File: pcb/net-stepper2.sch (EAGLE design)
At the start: 37 parts, among them IC2 CP2104, J1 MICRO-USB, J2 POWER_JACKPTH_LOCK, J3 ENCODER, J4 ENDSTOP2, J5 ENDSTOP1, J6 STEPER, Q1 600mA/40V, Q2 600mA/40V, U1 L6470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

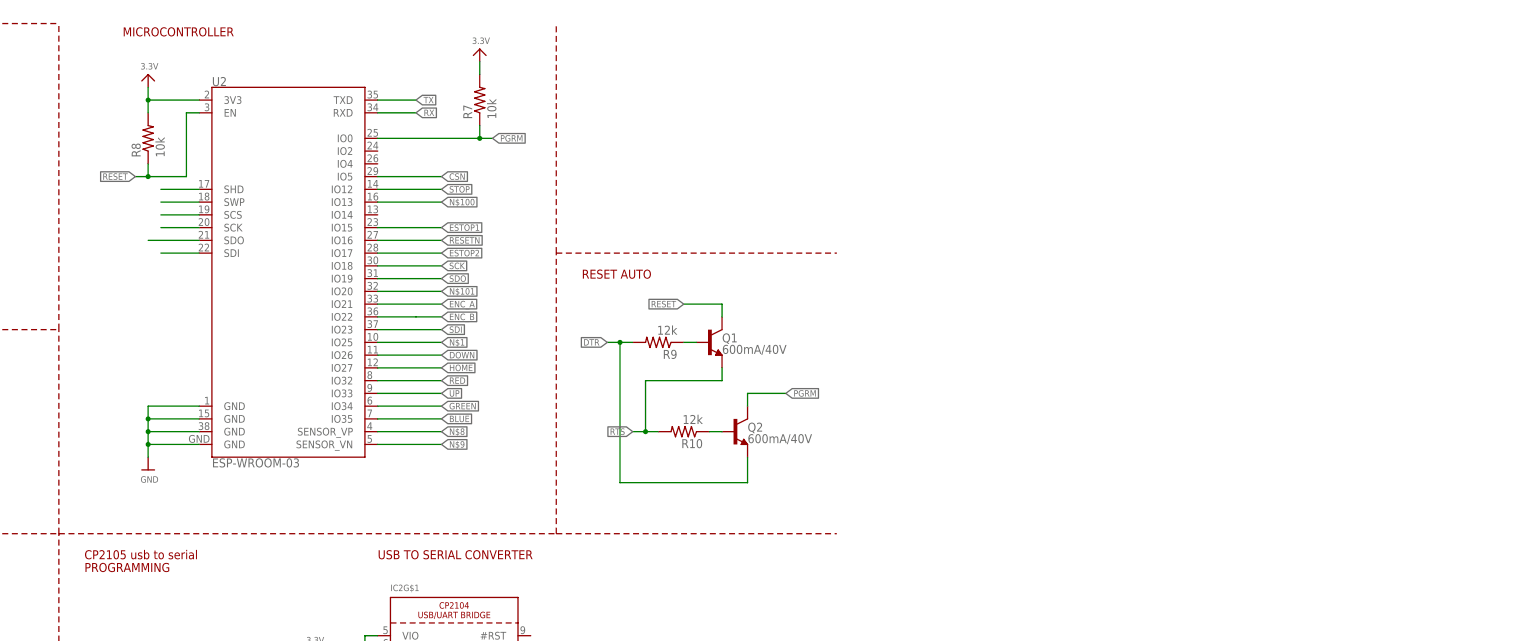
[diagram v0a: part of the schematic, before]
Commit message: replaced esp32 component
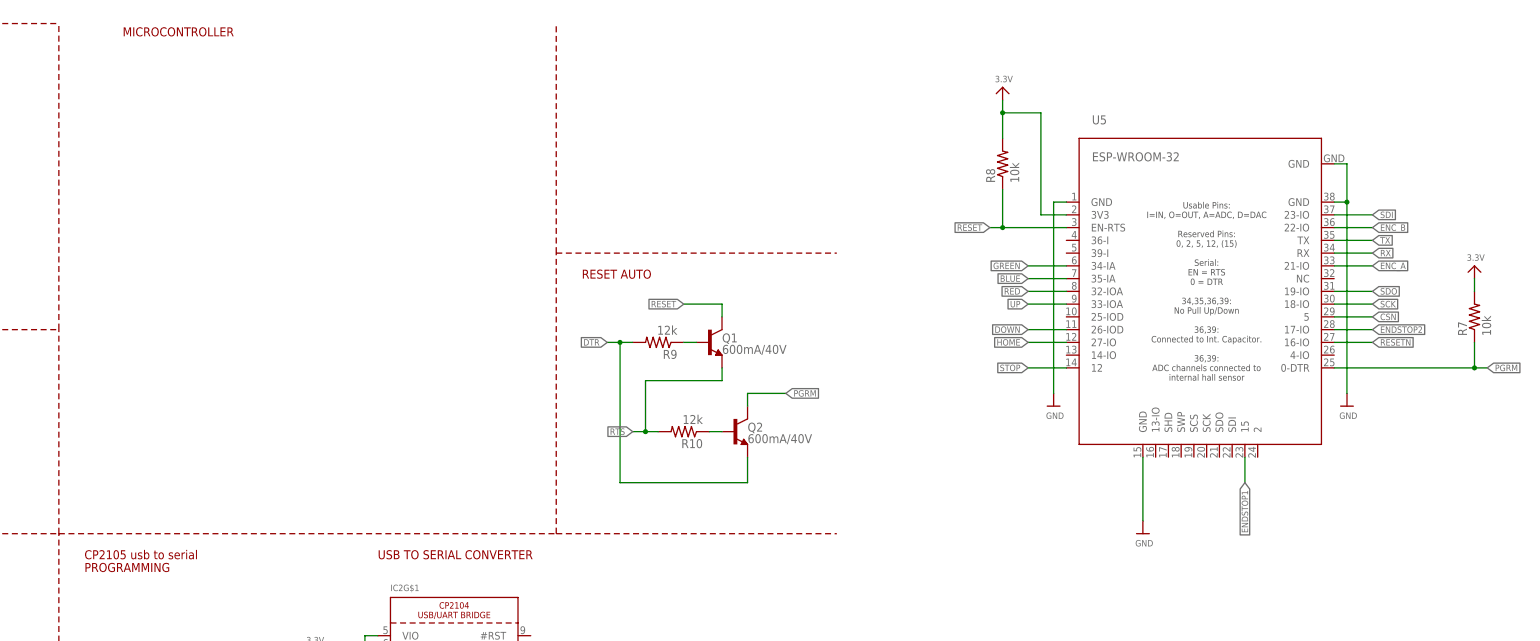
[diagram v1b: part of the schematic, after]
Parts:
- removed U2: ESP-WROOM-03, esp32:ESP-WROOM-03
- added U5: ESP-WROOM-32, esp32:ESP-WROOM-32
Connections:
- removed net ESTOP1: U2.IO15
- removed net ESTOP2: U2.IO17
- removed net N$1: U2.IO25
- removed net N$10: U2.SDI
- removed net N$100: U2.IO13
- removed net N$101: U2.IO20
- removed net N$2: U2.SHD
- removed net N$3: U2.SWP
- removed net N$4: U2.SCS
- removed net N$5: U2.SCK
- removed net N$6: U2.SDO
- removed net N$8: U2.SENSOR_VP
- removed net N$9: U2.SENSOR_VN
- net 3.3V: now also U5.3V3; no longer U2.3V3
- net BLUE: now also U5.35-IA; no longer U2.IO35
- net CSN: now also U5.5; no longer U2.IO5
- net DOWN: now also U5.26-IOD; no longer U2.IO26
- net ENC_A: now also U5.21-IO; no longer U2.IO21
- net ENC_B: now also U5.22-IO; no longer U2.IO22
- net ENDSTOP1: now also U5.15
- net ENDSTOP2: now also U5.17-IO
- net GND: now also U5.GND, U5.GND@1, U5.GND@15, U5.GND@38; no longer U2.GND, U2.GND@1, U2.GND@15, U2.GND@38
- net GREEN: now also U5.34-IA; no longer U2.IO34
- net HOME: now also U5.27-IO; no longer U2.IO27
- net PGRM: now also U5.0-DTR; no longer U2.IO0
- net RED: now also U5.32-IOA; no longer U2.IO32
- net RESET: now also U5.EN-RTS; no longer U2.EN
- net RESETN: now also U5.16-IO; no longer U2.IO16
- net RX: now also U5.RX; no longer U2.RXD
- net SCK: now also U5.18-IO; no longer U2.IO18
- net SDI: now also U5.23-IO; no longer U2.IO23
- net SDO: now also U5.19-IO; no longer U2.IO19
- net STOP: now also U5.12; no longer U2.IO12
- net TX: now also U5.TX; no longer U2.TXD
- net UP: now also U5.33-IOA; no longer U2.IO33
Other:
- moved on the sheet: R7, R8

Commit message: removed unused signals
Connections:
- removed net NC: J3.4
- removed net OSCIN: U1.OSCIN
- removed net OSCOUT: U1.OSCOUT
- removed net STCK: U1.STCK

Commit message: reorganized schematics
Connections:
- net ENDSTOP1 renamed END_STOP_1
- net ENDSTOP2 renamed END_STOP_2
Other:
- note added: "STEPPER CONTROLLER"
- note removed: "CP2105 usb to serial"
- note removed: "PROGRAMMING"
- note removed: "Status"
- moved on the sheet: C1, C2, C5, C6, C8, IC2G$1, J1, J3, J4, J5, J6, Q1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

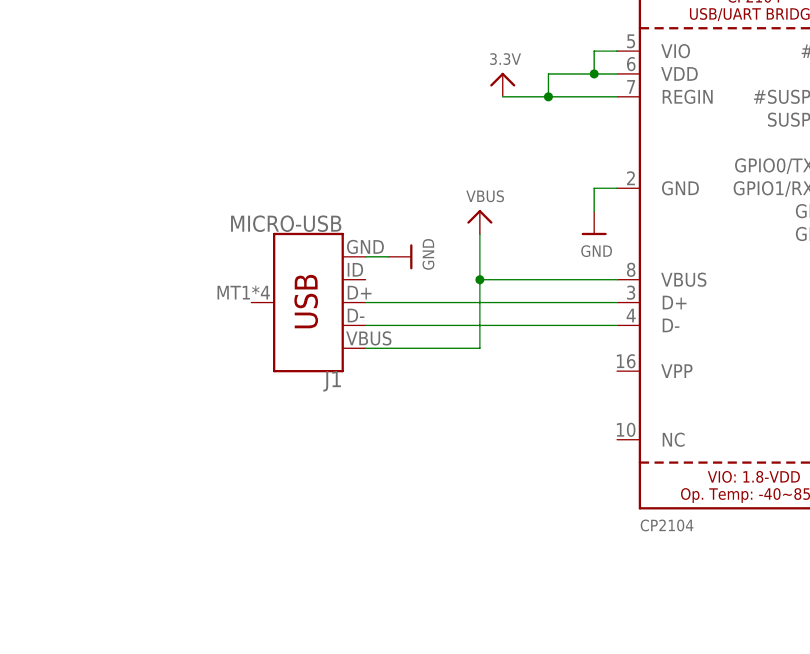
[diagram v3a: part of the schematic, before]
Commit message: connect usb mounting pins to ground
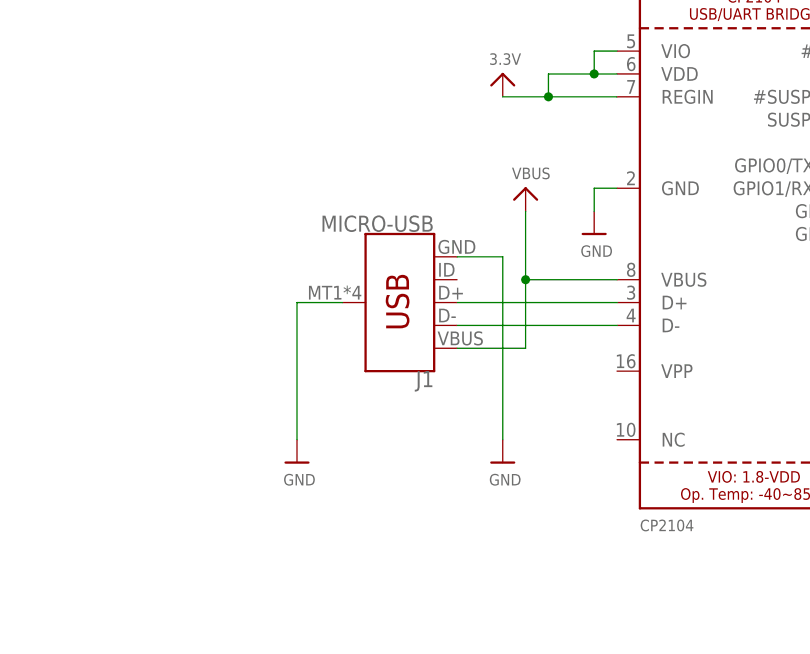
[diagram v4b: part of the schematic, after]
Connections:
- net GND: now also J1.SHIELD
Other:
- moved on the sheet: J1
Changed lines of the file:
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@@
 <part name="P+3" library="SparkFun-Aesthetics" deviceset="3.3V" device=""/>
 <part name="GND1" library="SparkFun" deviceset="GND" device=""/>
+<part name="U$7" library="microbuilder" deviceset="GND" device=""/>
 </parts>
 <sheets>
@@
 <instance part="S3" gate="G$1" x="134.62" y="7.62"/>
 <instance part="IC2" gate="G$1" x="490.22" y="121.92"/>
-<instance part="U$33" gate="G$1" x="452.12" y="119.38" rot="R90"/>
+<instance part="U$33" gate="G$1" x="462.28" y="96.52"/>
 <instance part="U$34" gate="G$1" x="472.44" y="121.92"/>
-<instance part="U$36" gate="G$1" x="459.74" y="124.46"/>
+<instance part="U$36" gate="G$1" x="464.82" y="127"/>
 <instance part="U$38" gate="G$1" x="462.28" y="139.7"/>
-<instance part="J1" gate="G$1" x="441.96" y="114.3" rot="R180"/>
+<instance part="J1" gate="G$1" x="452.12" y="114.3" rot="R180"/>
 <instance part="U3" gate="G$1" x="203.2" y="10.16" rot="R90"/>
 <instance part="U$26" gate="G$1" x="195.58" y="15.24"/>
@@
 <instance part="P+3" gate="G$1" x="109.22" y="185.42"/>
 <instance part="GND1" gate="1" x="30.48" y="0"/>
+<instance part="U$7" gate="G$1" x="439.42" y="96.52"/>
 </instances>
 <busses>
@@
 <pinref part="U$33" gate="G$1" pin="GND"/>
 <pinref part="J1" gate="G$1" pin="GND"/>
-<wire x1="447.04" y1="119.38" x2="449.58" y2="119.38" width="0.1524" layer="91"/>
+<wire x1="457.2" y1="119.38" x2="462.28" y2="119.38" width="0.1524" layer="91"/>
+<wire x1="462.28" y1="119.38" x2="462.28" y2="99.06" width="0.1524" layer="91"/>
 </segment>
 <segment>
@@
 <pinref part="U5" gate="G$1" pin="GND@38"/>
 <wire x1="345.44" y1="152.4" x2="347.98" y2="152.4" width="0.1524" layer="91"/>
+</segment>
+<segment>
+<pinref part="J1" gate="G$1" pin="SHIELD"/>
+<wire x1="444.5" y1="114.3" x2="439.42" y2="114.3" width="0.1524" layer="91"/>
+<pinref part="U$7" gate="G$1" pin="GND"/>
+<wire x1="439.42" y1="99.06" x2="439.42" y2="114.3" width="0.1524" layer="91"/>
 </segment>
 </net>
@@
 <segment>
 <pinref part="IC2" gate="G$1" pin="VBUS"/>
-<wire x1="459.74" y1="116.84" x2="474.98" y2="116.84" width="0.1524" layer="91"/>
+<wire x1="464.82" y1="116.84" x2="474.98" y2="116.84" width="0.1524" layer="91"/>
 <pinref part="U$36" gate="G$1" pin="VBUS"/>
-<wire x1="459.74" y1="116.84" x2="459.74" y2="121.92" width="0.1524" layer="91"/>
+<wire x1="464.82" y1="116.84" x2="464.82" y2="124.46" width="0.1524" layer="91"/>
 <pinref part="J1" gate="G$1" pin="VBUS"/>
-<wire x1="447.04" y1="109.22" x2="459.74" y2="109.22" width="0.1524" layer="91"/>
-<wire x1="459.74" y1="109.22" x2="459.74" y2="116.84" width="0.1524" layer="91"/>
-<junction x="459.74" y="116.84"/>
+<wire x1="457.2" y1="109.22" x2="464.82" y2="109.22" width="0.1524" layer="91"/>
+<wire x1="464.82" y1="109.22" x2="464.82" y2="116.84" width="0.1524" layer="91"/>
+<junction x="464.82" y="116.84"/>
 </segment>
 </net>
@@
 <pinref part="IC2" gate="G$1" pin="D+"/>
 <pinref part="J1" gate="G$1" pin="D+"/>
-<wire x1="447.04" y1="114.3" x2="474.98" y2="114.3" width="0.1524" layer="91"/>
+<wire x1="457.2" y1="114.3" x2="474.98" y2="114.3" width="0.1524" layer="91"/>
 </segment>
 </net>
@@
 <pinref part="IC2" gate="G$1" pin="D-"/>
 <pinref part="J1" gate="G$1" pin="D-"/>
-<wire x1="447.04" y1="111.76" x2="474.98" y2="111.76" width="0.1524" layer="91"/>
-</segment>
-</net>
+<wire x1="457.2" y1="111.76" x2="474.98" y2="111.76" width="0.1524" layer="91"/>
+</segment>
+</net>

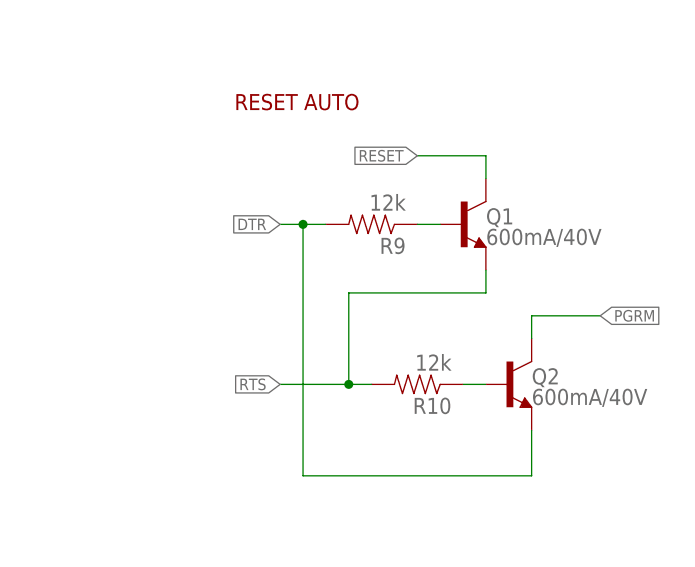
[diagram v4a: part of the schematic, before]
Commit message: changed pull resistors to 10k in order remove one resistor family
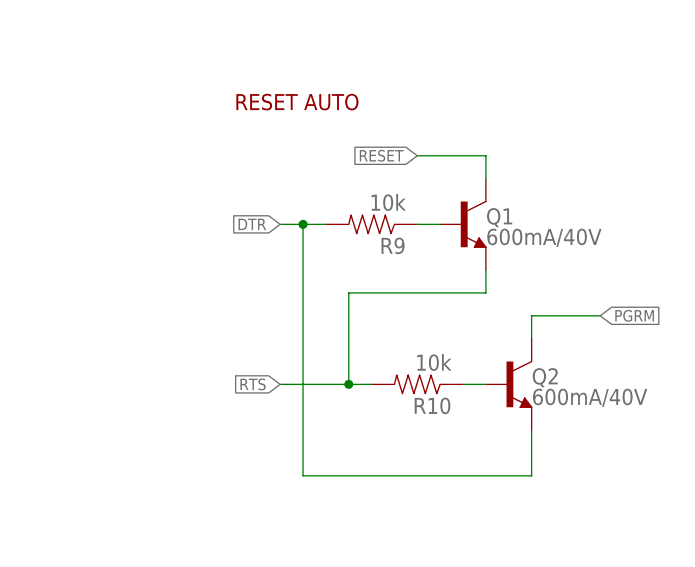
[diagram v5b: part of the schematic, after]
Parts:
- R10, R9: value 12k -> 10k
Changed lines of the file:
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@@
 <part name="U$22" library="microbuilder" deviceset="3.3V" device=""/>
 <part name="R8" library="SparkFun-Passives" deviceset="RESISTOR" device="0603-RES" value="10k"/>
-<part name="R9" library="SparkFun-Passives" deviceset="RESISTOR" device="0603-RES" value="12k"/>
-<part name="R10" library="SparkFun-Passives" deviceset="RESISTOR" device="0603-RES" value="12k"/>
+<part name="R9" library="SparkFun-Passives" deviceset="RESISTOR" device="0603-RES" value="10k"/>
+<part name="R10" library="SparkFun-Passives" deviceset="RESISTOR" device="0603-RES" value="10k"/>
 <part name="U$14" library="microbuilder" deviceset="GND" device=""/>
 <part name="J3" library="SparkFun-Connectors" deviceset="M05" device="PTH" value="ENCODER"/>
